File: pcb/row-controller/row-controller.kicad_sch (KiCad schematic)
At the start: 36 parts, among them IC1 INA220BIDGSR, IC2 THVD1420DR, IC3 THVD1420DR, J1 Power, J2 5555140-2, J4 5555140-2, U1 XAIO ESP32-C3, U2 R-78E5.0-0.5

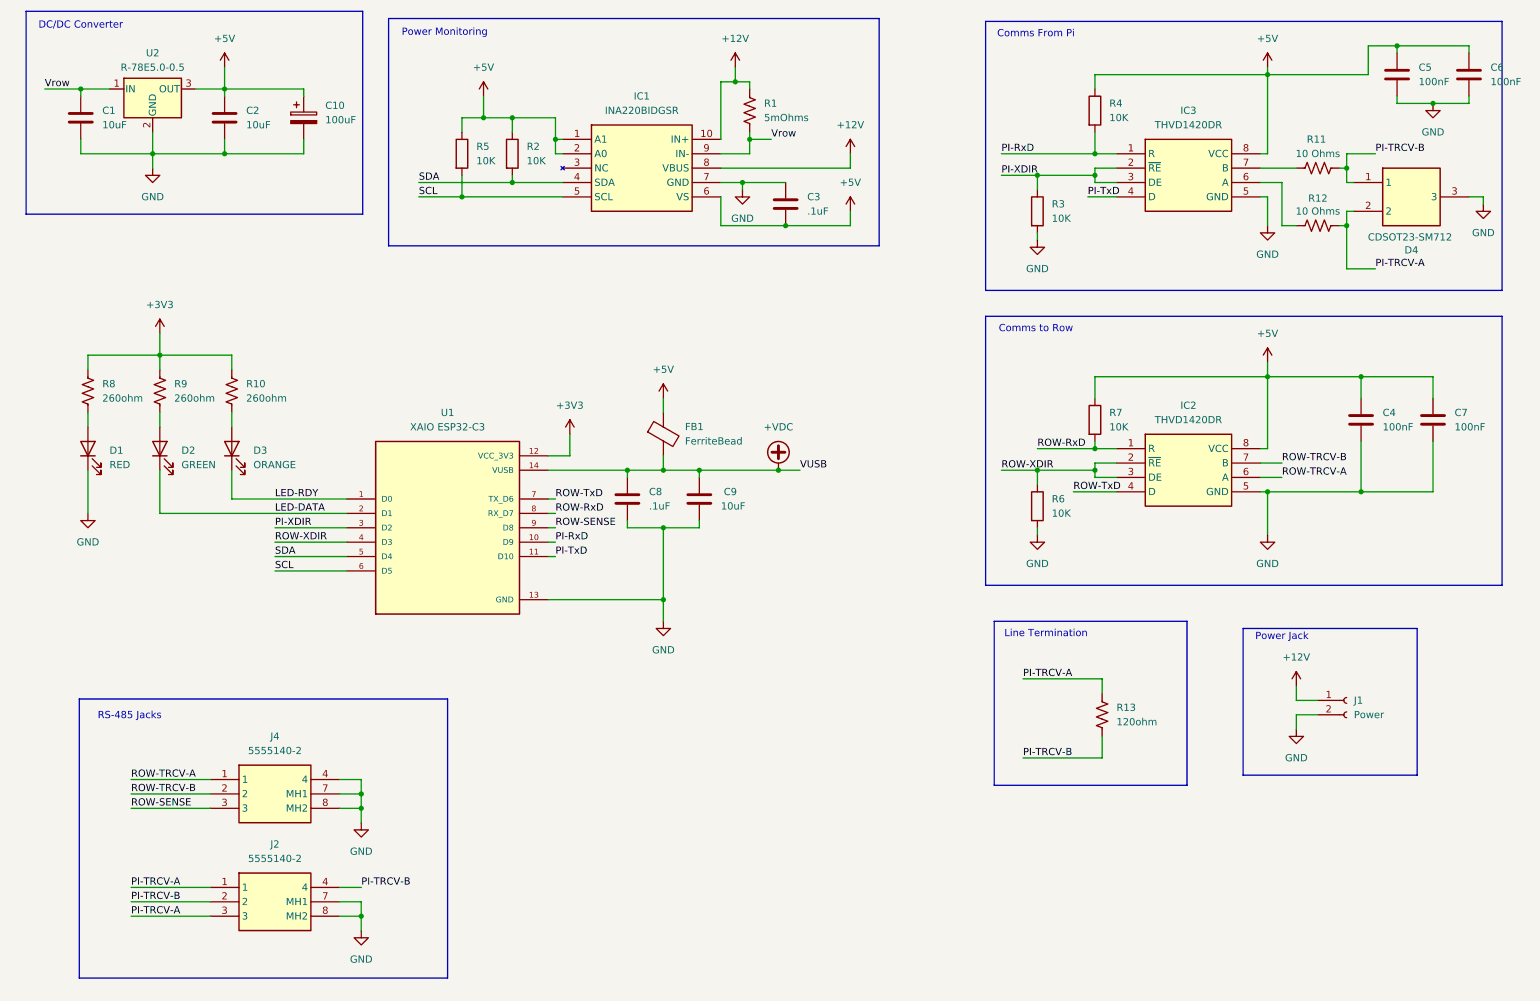
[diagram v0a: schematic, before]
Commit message: Removed the ferrite bead, updated power symbols.
Not convinced I need the beads, can do some testing to confirm this when I have test boards
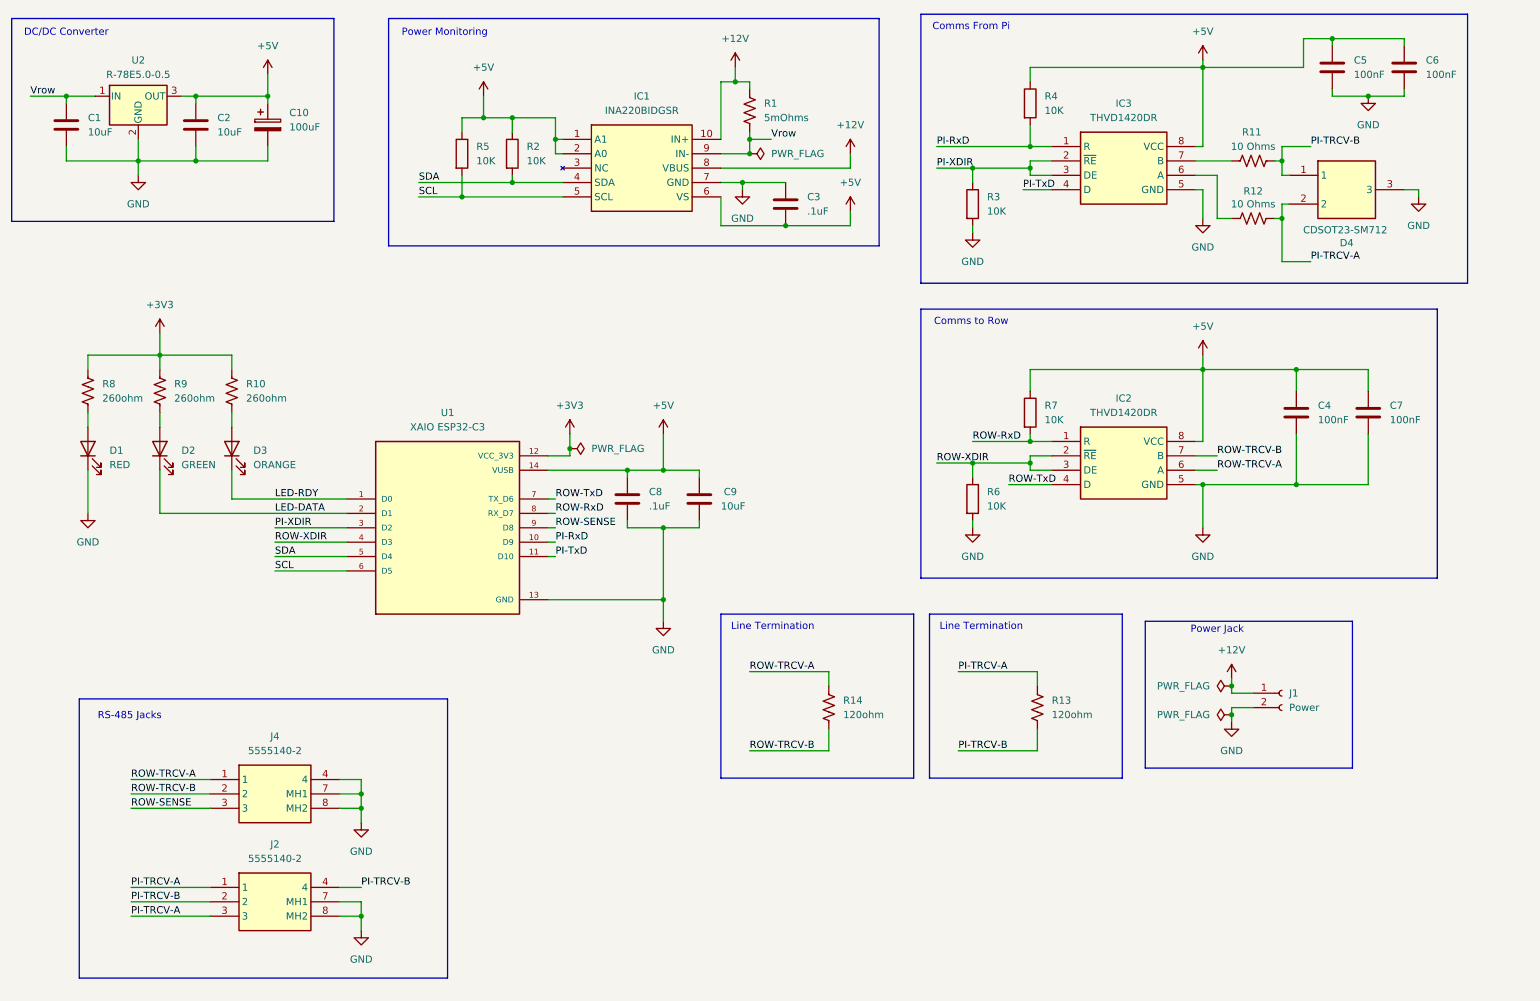
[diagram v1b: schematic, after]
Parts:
- removed FB1: FerriteBead, Inductor_SMD:L_0805_2012Metric_Pad1.15x1.40mm_HandSolder, symbol Device:FerriteBead
- added R14: 120ohm, Resistor_SMD:R_0805_2012Metric_Pad1.20x1.40mm_HandSolder, symbol Device:R_US
- D1, D2, D3: footprint (none) -> LED_SMD:LED_0805_2012Metric_Pad1.15x1.40mm_HandSolder
- D4: footprint SOT95P230X117-3N -> Garth:SOT95P230X117-3N
- IC1: footprint SOP50P490X110-10N -> INA220BIDGSR:SOP50P490X110-10N
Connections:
- net +VDC is gone; now on net +5V: C8.1, C9.1, U1.14 (VUSB)
- net ROW-TRCV-A: now also R14.1
- net ROW-TRCV-B: now also R14.2
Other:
- moved on the sheet: C1, C10, C2, C4, C5, C6, C7, D4, IC2, IC3, J1, R11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

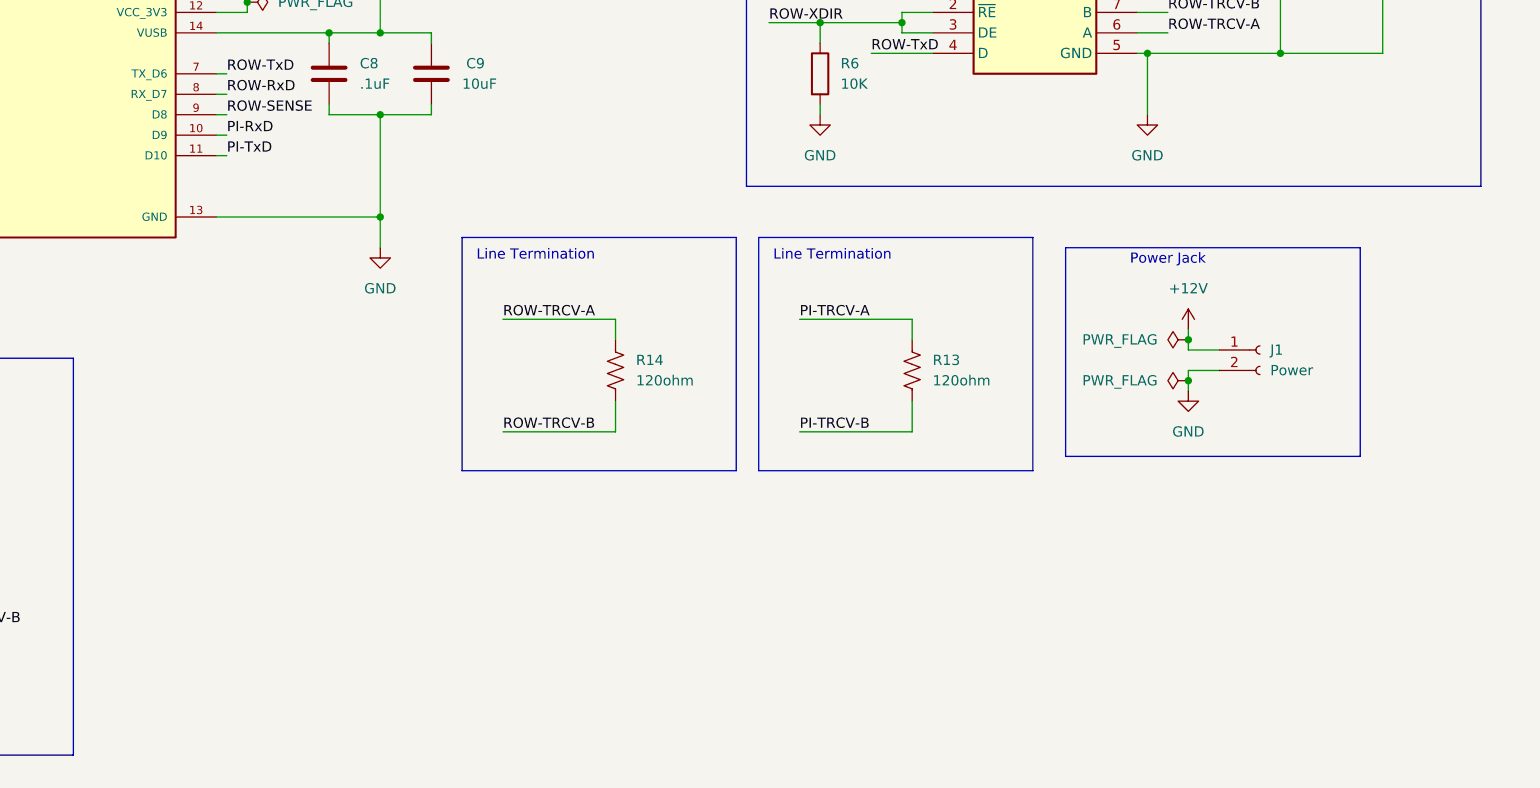
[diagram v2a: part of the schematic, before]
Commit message: Additon of second power jack, plus notes/todos for things that need updating
Checkpointing here since this is what the last fab got and I want to be able to come back to it
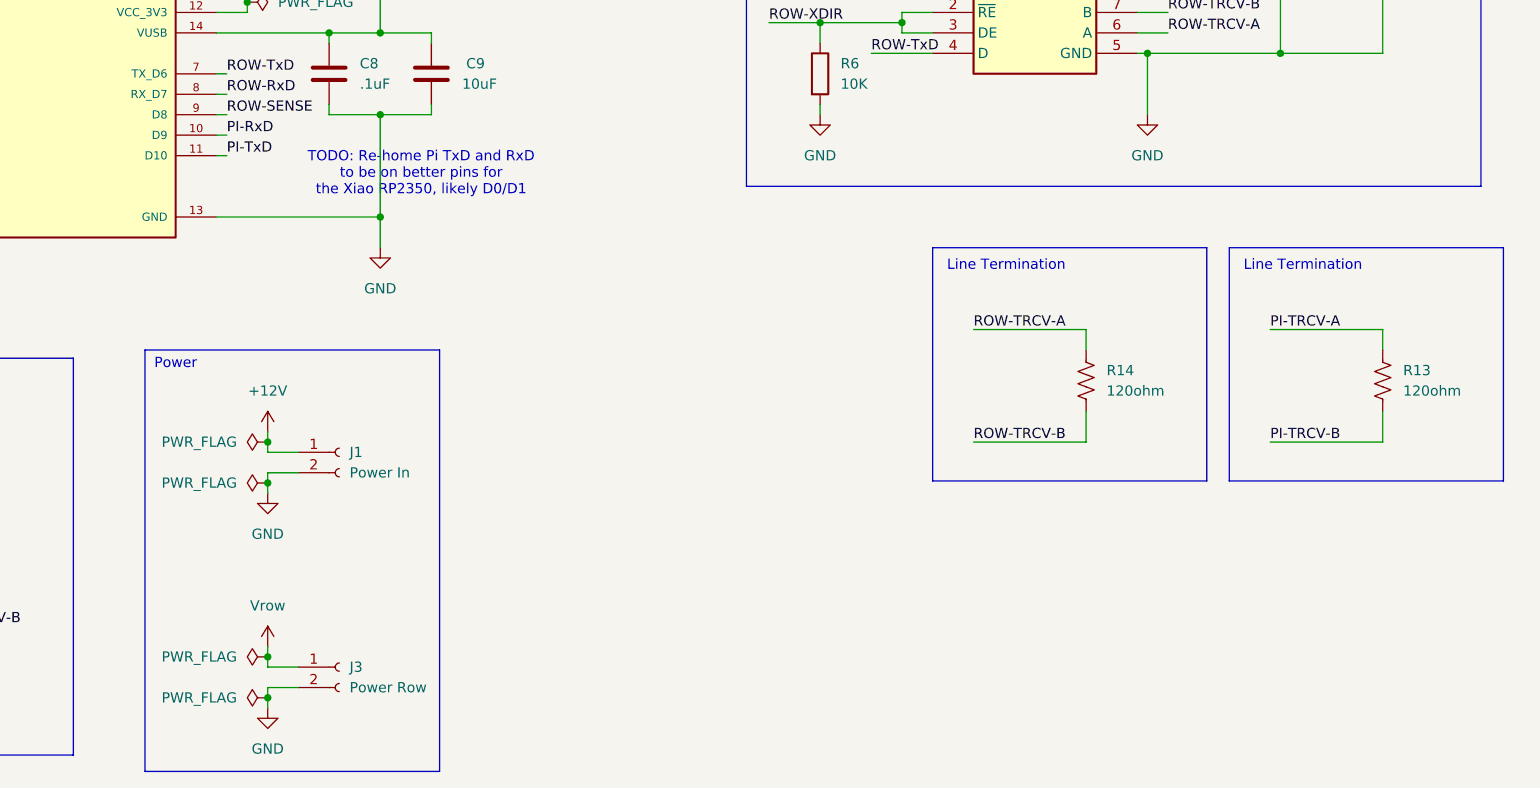
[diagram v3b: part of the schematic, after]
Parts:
- added J3: Power Row, Connector_JST:JST_XH_S2B-XH-A_1x02_P2.50mm_Horizontal, symbol Connector:Conn_01x02_Socket
- J1: value Power -> Power In
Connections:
- net GND: now also J3.2 (Pin_2)
- net Vrow: now also J3.1 (Pin_1)
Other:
- note added: "Power"
- note added: "TODO: Re-home Pi TxD and RxD to be on better pins for the Xiao RP2350, likely D0/D1"
- note removed: "Power Jack"
- moved on the sheet: J1, R13, R14
